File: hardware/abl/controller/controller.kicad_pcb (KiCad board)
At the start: 4 copper layers, 56.2 x 74 mm, 39 parts, among them IC2 FXL6408UMX, IC3 VEML6040A3OG, IC4 FXL6408UMX, J1 SFW20S-2STE1LF, J2 Conn_02x05_Odd_Even, J3 Conn_02x05_Odd_Even, J4 PRT-14417, J5 Conn_02x05_Odd_Even, Q2 AO3401A, Q4 AO3401A, U1 INA219AxD, U2 TXB0104RUT

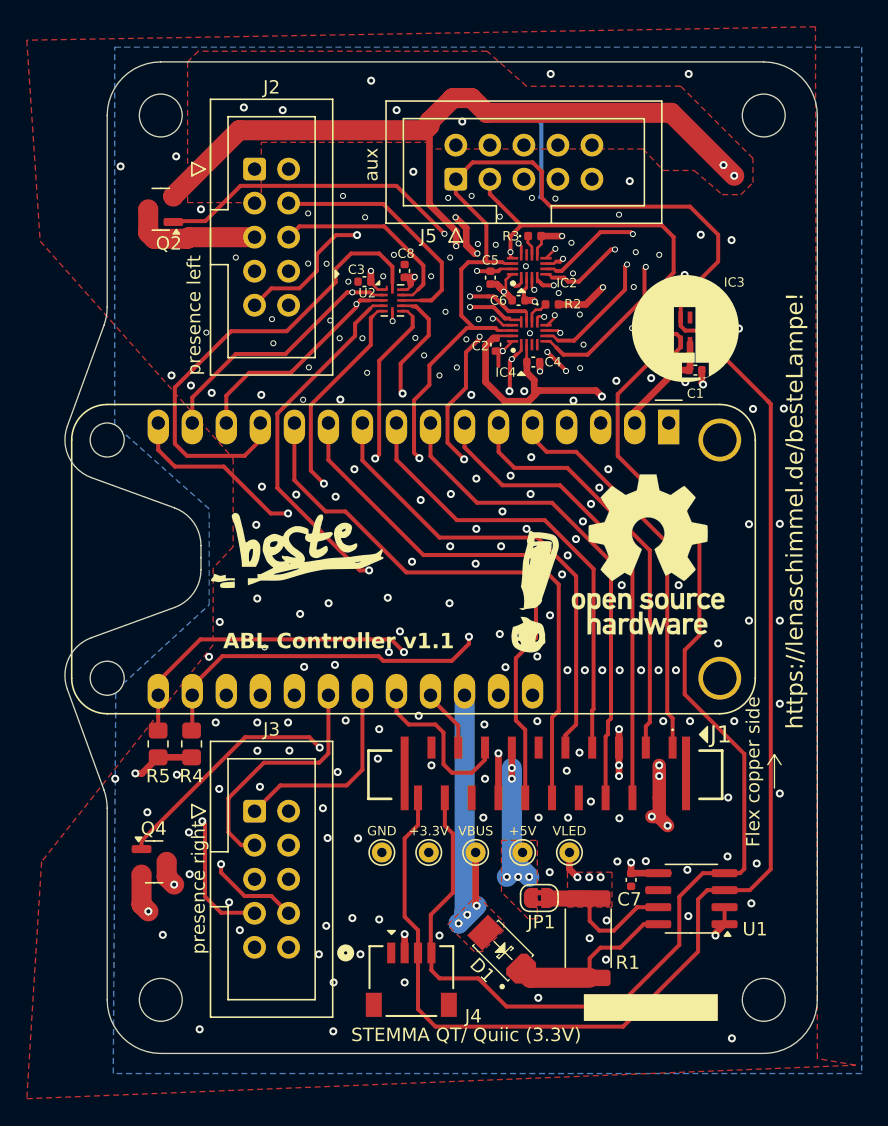
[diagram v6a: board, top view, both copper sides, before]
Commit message: Fix 5V power supply for Feather.
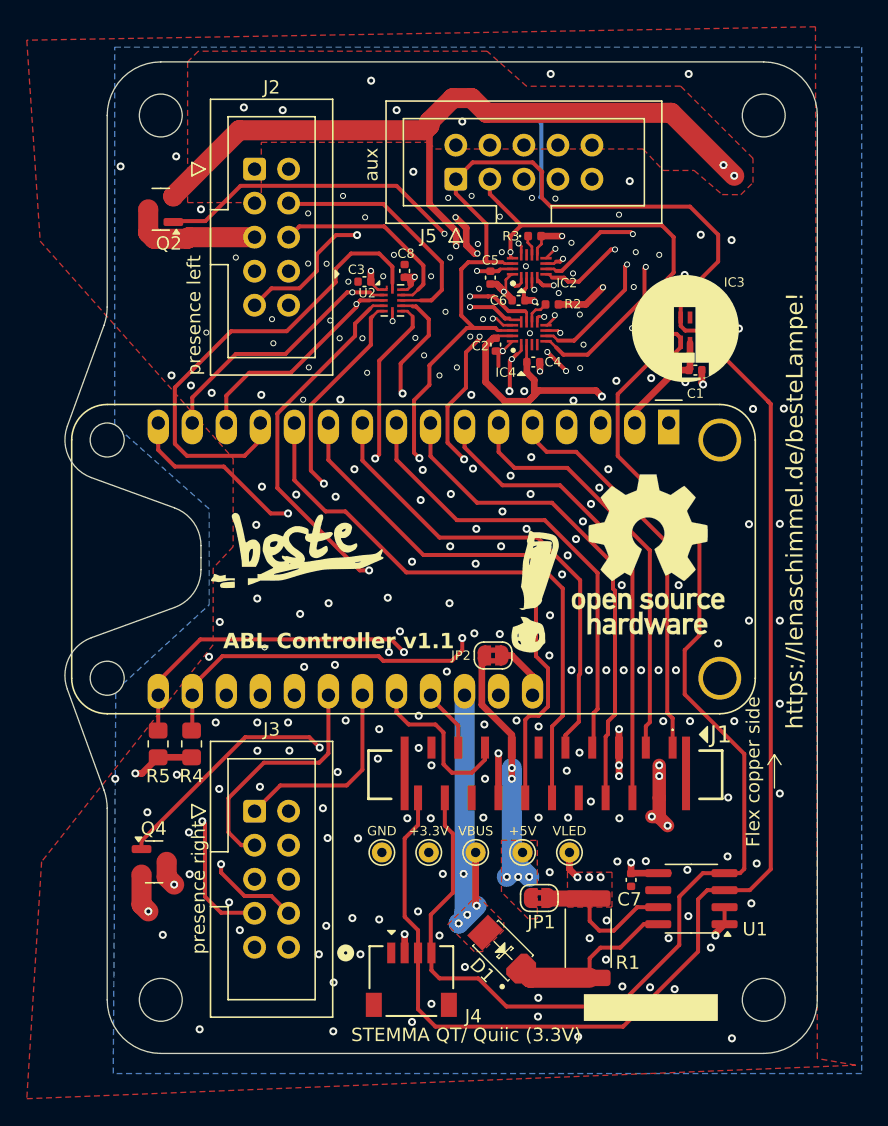
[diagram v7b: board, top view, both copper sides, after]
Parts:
- added JP2: SolderJumper_2_Bridged, Jumper:SolderJumper-2_P1.3mm_Bridged2Bar_RoundedPad1.0x1.5mm, F.Cu at (91.8, 95.3)
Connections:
- A1 pad 28: unconnected-(A1-VBAT-Pad28) -> +BATT
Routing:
- net +5V: track 95.1 -> 103.3 mm
- net +BATT: track 0.00 -> 4.36 mm
- net /i8: track 42.4 -> 42.9 mm
- net GND: track 22.9 -> 23.0 mm, vias 201 -> 219

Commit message: Change pins 13 and 16 to fix bootloader problem. Nees better docu.
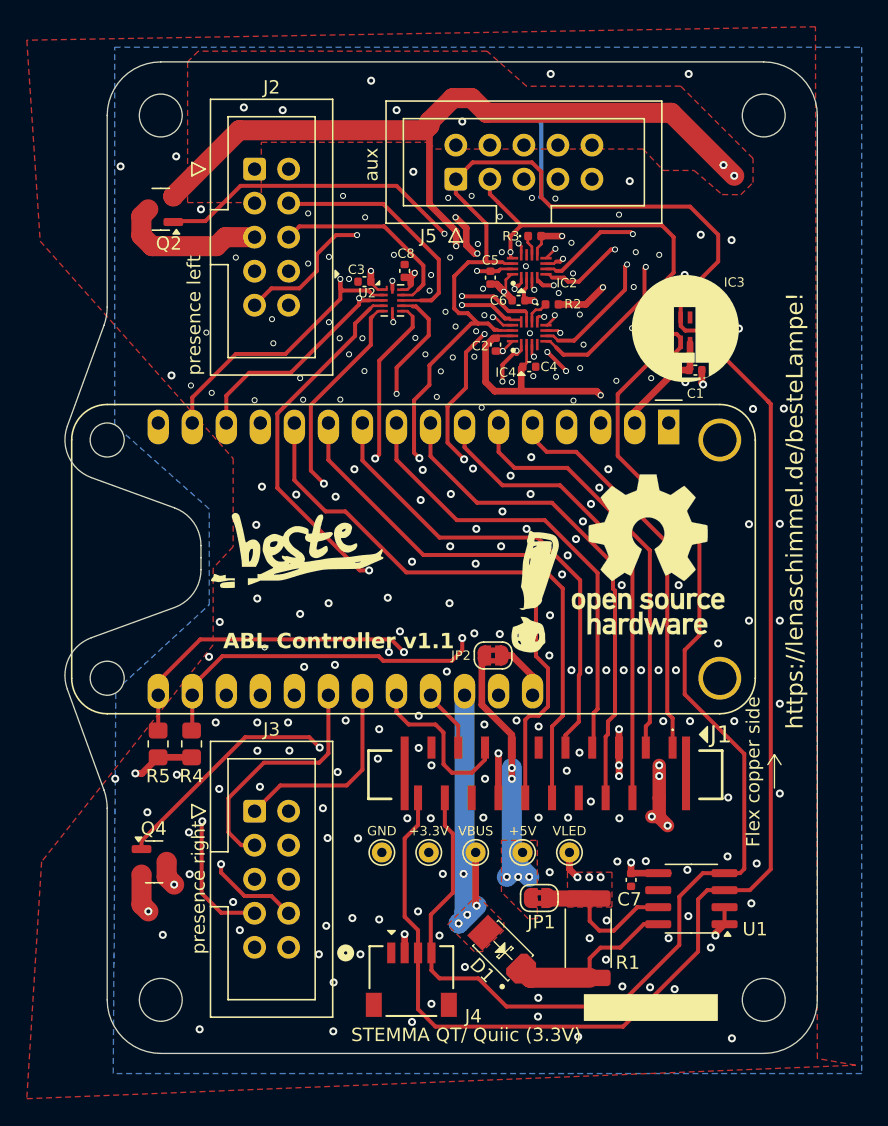
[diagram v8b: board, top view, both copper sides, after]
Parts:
- moved C4 0.46 mm to (94.5, 73.8)
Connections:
- A1 pad 13: /EN_UART -> /GP_INT
- A1 pad 16: /GP_INT -> unconnected-(A1-SPARE-Pad16)
- IC4 pad 3: /FX_3_7 -> /EN_UART
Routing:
- net /GP_INT: track 49.7 -> 31.1 mm, vias 4 -> 3
- net /EN_UART: track 36.3 -> 18.6 mm, vias 0 -> 2
- net +3.3V: track 112.8 -> 110.2 mm
- net Net-(J2-Pin_5): track 9.93 -> 11.2 mm
- net /SDA: track 197.2 -> 198.1 mm
- net /FX_3_1: track 20.8 -> 21.6 mm
- net GND: track 23.0 -> 23.7 mm, vias 219 -> 224
- net /TX_L: track 33.4 -> 34.1 mm
- net /FX_3_2: track 73.3 -> 72.7 mm
